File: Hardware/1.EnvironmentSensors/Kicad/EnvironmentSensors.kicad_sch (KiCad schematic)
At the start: 16 parts, among them J2 Conn_01x10_Pin, U1 SHT4x, U2 BME680, U3 LPS22HB

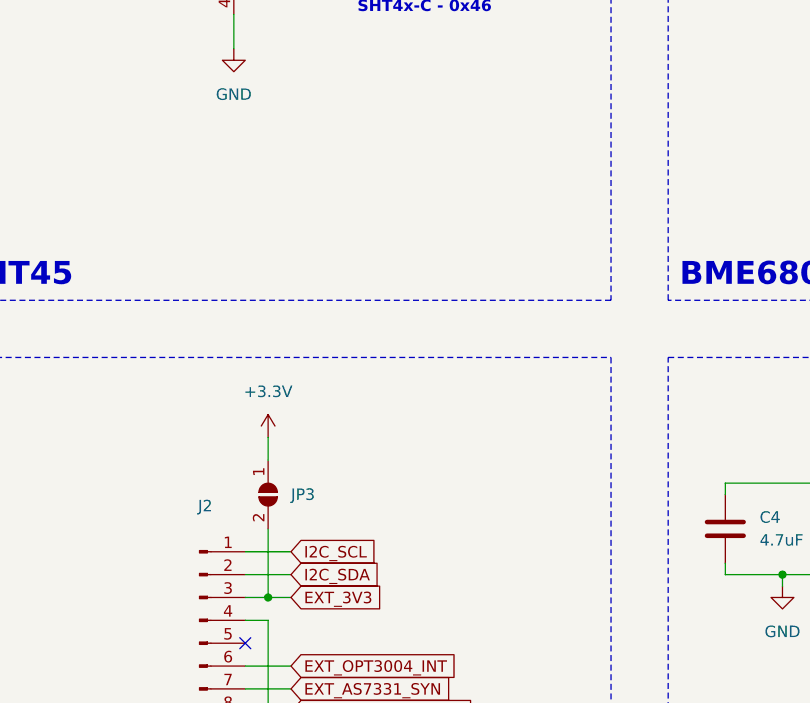
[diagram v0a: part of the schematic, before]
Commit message: Add SF2 filter to schematic
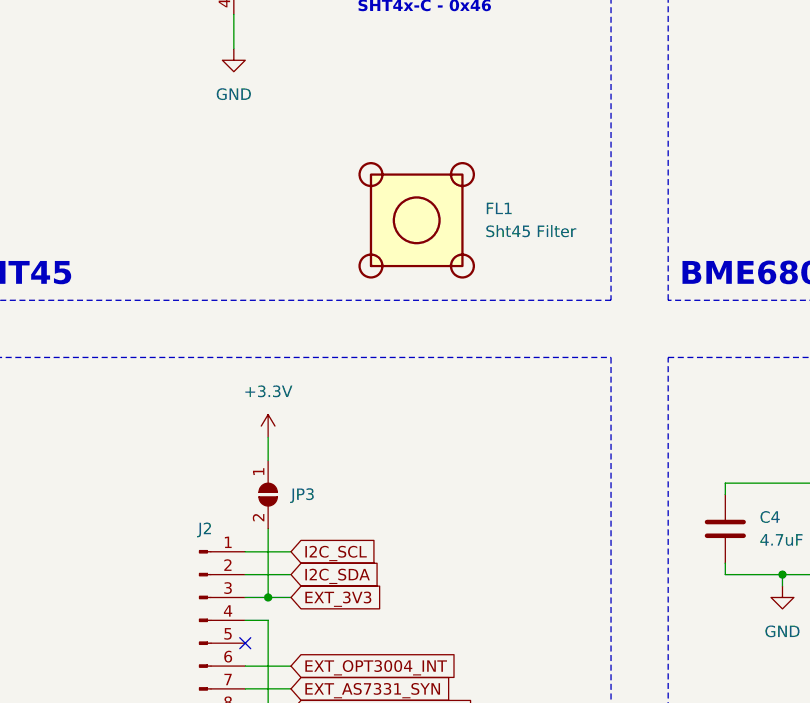
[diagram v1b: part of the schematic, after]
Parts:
- added FL1: Sht45 Filter, FIL_SF2_FILTER_CAP:FIL_SF2_FILTER_CAP, symbol SF2_FILTER_CAP:SF2_FILTER_CAP
- J2: footprint Connector_JST:JST_PH_S10B-PH-K_1x10_P2.00mm_Horizontal -> Connector_JST:JST_PH_B10B-PH-K_1x10_P2.00mm_Vertical
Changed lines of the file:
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@@
   (title_block
     (title "Enviroment Sensors")
-    (date "2023-07-30")
+    (date "2023-08-05")
     (rev "A")
   )
@@
     (pin "2")
     (instances
-      (project "EnviromentSensors"
+      (project "EnvironmentSensors"
         (path "/fc1a0c50-39ba-4cf6-ad6f-af313c028135"
           (reference "JP1") (unit 1)
@@
     (pin "1")
     (instances
-      (project "EnviromentSensors"
+      (project "EnvironmentSensors"
         (path "/fc1a0c50-39ba-4cf6-ad6f-af313c028135"
           (reference "#PWR08") (unit 1)
@@
     (pin "1")
     (instances
-      (project "EnviromentSensors"
+      (project "EnvironmentSensors"
         (path "/fc1a0c50-39ba-4cf6-ad6f-af313c028135"
           (reference "#PWR07") (unit 1)
@@
     (pin "1")
     (instances
-      (project "EnviromentSensors"
+      (project "EnvironmentSensors"
         (path "/fc1a0c50-39ba-4cf6-ad6f-af313c028135"
           (reference "#FLG02") (unit 1)
@@
     (pin "2")
     (instances
-      (project "EnviromentSensors"
+      (project "EnvironmentSensors"
         (path "/fc1a0c50-39ba-4cf6-ad6f-af313c028135"
           (reference "C1") (unit 1)
@@
     (pin "1")
     (instances
-      (project "EnviromentSensors"
+      (project "EnvironmentSensors"
         (path "/fc1a0c50-39ba-4cf6-ad6f-af313c028135"
           (reference "#PWR02") (unit 1)
@@
     )
   )
+  (symbol (lib_id "SF2_FILTER_CAP:SF2_FILTER_CAP") (at 133.35 73.66 0) (unit 1)
+    (in_bom yes) (on_board yes) (dnp no) (fields_autoplaced)
+    (property "Reference" "FL1" (at 140.97 72.39 0)
+      (effects (font (size 1.27 1.27)) (justify left))
+    )
+    (property "Value" "Sht45 Filter" (at 140.97 74.93 0)
+      (effects (font (size 1.27 1.27)) (justify left))
+    )
+    (property "Footprint" "FIL_SF2_FILTER_CAP:FIL_SF2_FILTER_CAP" (at 133.35 73.66 0)
+      (effects (font (size 1.27 1.27)) (justify bottom) hide)
+    )
+    (property "Datasheet" "" (at 133.35 73.66 0)
+      (effects (font (size 1.27 1.27)) hide)
+    )
+    (property "MANUFACTURER" "Sensirion" (at 133.35 73.66 0)
+      (effects (font (size 1.27 1.27)) (justify bottom) hide)
+    )
+    (instances
+      (project "EnvironmentSensors"
+        (path "/fc1a0c50-39ba-4cf6-ad6f-af313c028135"
+          (reference "FL1") (unit 1)
+        )
+      )
+    )
+  )
   (symbol (lib_id "power:GND") (at 173.99 114.3 0) (unit 1)
     (in_bom yes) (on_board yes) (dnp no) (fields_autoplaced)
@@
     (pin "1")
     (instances
-      (project "EnviromentSensors"
+      (project "EnvironmentSensors"
         (path "/fc1a0c50-39ba-4cf6-ad6f-af313c028135"
           (reference "#PWR014") (unit 1)
@@
     (pin "1")
     (instances
-      (project "EnviromentSensors"
+      (project "EnvironmentSensors"
         (path "/fc1a0c50-39ba-4cf6-ad6f-af313c028135"
           (reference "#PWR013") (unit 1)
@@
     (pin "1")
     (instances
-      (project "EnviromentSensors"
+      (project "EnvironmentSensors"
         (path "/fc1a0c50-39ba-4cf6-ad6f-af313c028135"
           (reference "#FLG01") (unit 1)
@@
     (pin "1")
     (instances
-      (project "EnviromentSensors"
+      (project "EnvironmentSensors"
         (path "/fc1a0c50-39ba-4cf6-ad6f-af313c028135"
           (reference "#PWR011") (unit 1)
@@
   (symbol (lib_id "Connector:Conn_01x10_Pin") (at 109.22 120.65 0) (unit 1)
     (in_bom yes) (on_board yes) (dnp no) (fields_autoplaced)
-    (property "Reference" "J2" (at 109.855 105.41 0)
+    (property "Reference" "J2" (at 109.855 107.95 0)
       (effects (font (size 1.27 1.27)))
     )
@@
         )
       )
-      (project "EnviromentSensors"
-        (path "/fc1a0c50-39ba-4cf6-ad6f-af313c028135"
-          (reference "J3") (unit 1)
+      (project "EnvironmentSensors"
+        (path "/fc1a0c50-39ba-4cf6-ad6f-af313c028135"
+          (reference "J2") (unit 1)
         )
       )
@@
     (pin "1")
     (instances
-      (project "EnviromentSensors"
+      (project "EnvironmentSensors"
         (path "/fc1a0c50-39ba-4cf6-ad6f-af313c028135"
           (reference "#PWR04") (unit 1)
@@
       (effects (font (size 1.27 1.27)) hide)
     )
-    (property "Footprint" "Connector_JST:JST_PH_S10B-PH-K_1x10_P2.00mm_Horizontal" (at 26.67 52.07 0)
+    (property "Footprint" "Connector_JST:JST_PH_B10B-PH-K_1x10_P2.00mm_Vertical" (at 26.67 52.07 0)
       (effects (font (size 1.27 1.27)) hide)
     )
@@
         )
       )
-      (project "EnviromentSensors"
+      (project "EnvironmentSensors"
         (path "/fc1a0c50-39ba-4cf6-ad6f-af313c028135"
           (reference "J1") (unit 1)
@@
     (pin "2")
     (instances
-      (project "EnviromentSensors"
+      (project "EnvironmentSensors"
         (path "/fc1a0c50-39ba-4cf6-ad6f-af313c028135"
           (reference "JP3") (unit 1)
@@
     (pin "1")
     (instances
-      (project "EnviromentSensors"
+      (project "EnvironmentSensors"
         (path "/fc1a0c50-39ba-4cf6-ad6f-af313c028135"
           (reference "#PWR015") (unit 1)
@@
     (pin "1")
     (instances
-      (project "EnviromentSensors"
+      (project "EnvironmentSensors"
         (path "/fc1a0c50-39ba-4cf6-ad6f-af313c028135"
           (reference "#PWR05") (unit 1)
@@
     (pin "2")
     (instances
-      (project "EnviromentSensors"
+      (project "EnvironmentSensors"
         (path "/fc1a0c50-39ba-4cf6-ad6f-af313c028135"
           (reference "R3") (unit 1)
@@
     (pin "1")
     (instances
-      (project "EnviromentSensors"
+      (project "EnvironmentSensors"
         (path "/fc1a0c50-39ba-4cf6-ad6f-af313c028135"
           (reference "#PWR09") (unit 1)
@@
     (pin "2")
     (instances
-      (project "EnviromentSensors"
+      (project "EnvironmentSensors"
         (path "/fc1a0c50-39ba-4cf6-ad6f-af313c028135"
           (reference "R2") (unit 1)
@@
     (pin "9")
     (instances
-      (project "EnviromentSensors"
+      (project "EnvironmentSensors"
         (path "/fc1a0c50-39ba-4cf6-ad6f-af313c028135"
           (reference "U3") (unit 1)
@@
     (pin "1")
     (instances
-      (project "EnviromentSensors"
+      (project "EnvironmentSensors"
         (path "/fc1a0c50-39ba-4cf6-ad6f-af313c028135"
           (reference "#PWR06") (unit 1)
@@
     (pin "1")
     (instances
-      (project "EnviromentSensors"
+      (project "EnvironmentSensors"
         (path "/fc1a0c50-39ba-4cf6-ad6f-af313c028135"
           (reference "#PWR012") (unit 1)
@@
         )
       )
-      (project "EnviromentSensors"
+      (project "EnvironmentSensors"
         (path "/fc1a0c50-39ba-4cf6-ad6f-af313c028135"
           (reference "#PWR018") (unit 1)
@@
     (pin "2")
     (instances
-      (project "EnviromentSensors"
+      (project "EnvironmentSensors"
         (path "/fc1a0c50-39ba-4cf6-ad6f-af313c028135"
           (reference "R1") (unit 1)
@@
     (pin "1")
     (instances
-      (project "EnviromentSensors"
+      (project "EnvironmentSensors"
         (path "/fc1a0c50-39ba-4cf6-ad6f-af313c028135"
           (reference "#PWR010") (unit 1)
@@
     (pin "2")
     (instances
-      (project "EnviromentSensors"
+      (project "EnvironmentSensors"
         (path "/fc1a0c50-39ba-4cf6-ad6f-af313c028135"
           (reference "C2") (unit 1)
@@
     (pin "8")
     (instances
-      (project "EnviromentSensors"
+      (project "EnvironmentSensors"
         (path "/fc1a0c50-39ba-4cf6-ad6f-af313c028135"
           (reference "U2") (unit 1)
@@
     (pin "2")
     (instances
-      (project "EnviromentSensors"
+      (project "EnvironmentSensors"
         (path "/fc1a0c50-39ba-4cf6-ad6f-af313c028135"
           (reference "R4") (unit 1)
@@
     (pin "1")
     (instances
-      (project "EnviromentSensors"
+      (project "EnvironmentSensors"
         (path "/fc1a0c50-39ba-4cf6-ad6f-af313c028135"
           (reference "#PWR016") (unit 1)
@@
     (pin "1")
     (instances
-      (project "EnviromentSensors"
+      (project "EnvironmentSensors"
         (path "/fc1a0c50-39ba-4cf6-ad6f-af313c028135"
           (reference "#PWR01") (unit 1)
@@
     (pin "2")
     (instances
-      (project "EnviromentSensors"
+      (project "EnvironmentSensors"
         (path "/fc1a0c50-39ba-4cf6-ad6f-af313c028135"
           (reference "C4") (unit 1)
@@
     (pin "1")
     (instances
-      (project "EnviromentSensors"
+      (project "EnvironmentSensors"
         (path "/fc1a0c50-39ba-4cf6-ad6f-af313c028135"
           (reference "#PWR017") (unit 1)
@@
     (pin "2")
     (instances
-      (project "EnviromentSensors"
+      (project "EnvironmentSensors"
         (path "/fc1a0c50-39ba-4cf6-ad6f-af313c028135"
           (reference "JP2") (unit 1)
@@
     (pin "1")
     (instances
-      (project "EnviromentSensors"
+      (project "EnvironmentSensors"
         (path "/fc1a0c50-39ba-4cf6-ad6f-af313c028135"
           (reference "#PWR03") (unit 1)
@@
     (pin "2")
     (instances
-      (project "EnviromentSensors"
+      (project "EnvironmentSensors"
         (path "/fc1a0c50-39ba-4cf6-ad6f-af313c028135"
           (reference "C3") (unit 1)
@@
     (pin "4")
     (instances
-      (project "EnviromentSensors"
+      (project "EnvironmentSensors"
         (path "/fc1a0c50-39ba-4cf6-ad6f-af313c028135"
           (reference "U1") (unit 1)

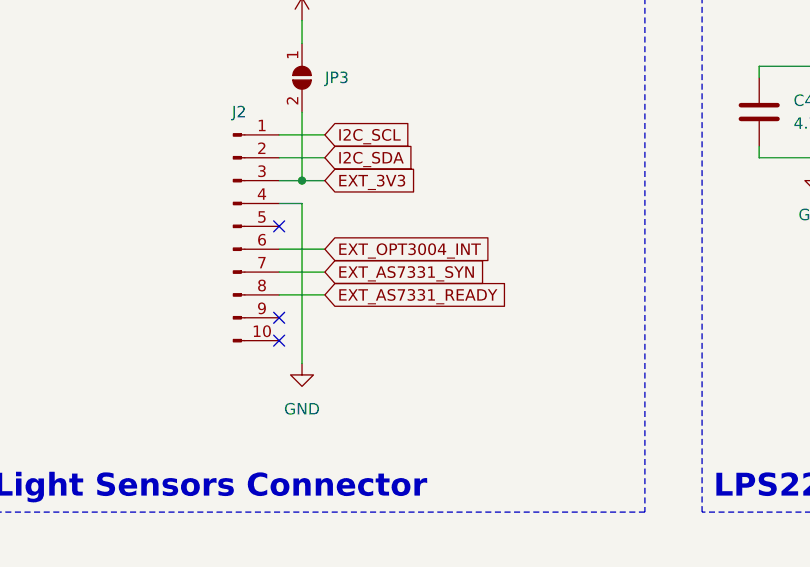
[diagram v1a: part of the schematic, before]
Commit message: Change footprint for connectors
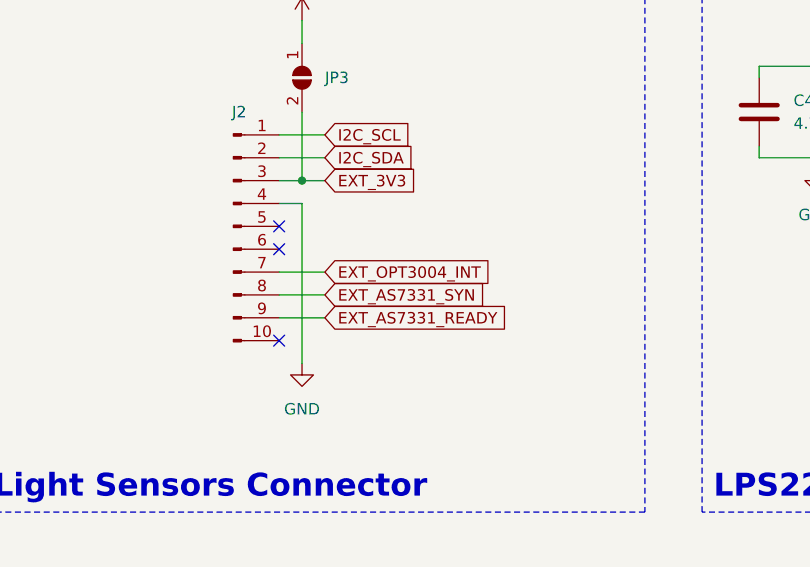
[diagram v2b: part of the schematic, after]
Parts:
- J2: footprint Connector_JST:JST_PH_B10B-PH-K_1x10_P2.00mm_Vertical -> Connector_JST:JST_PH_B10B-PH-SM4-TB_1x10-1MP_P2.00mm_Vertical
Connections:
- net EXT_AS7331_READY: now also J2.9 (Pin_9); no longer J2.8 (Pin_8)
- net EXT_AS7331_SYN: now also J2.8 (Pin_8); no longer J2.7 (Pin_7)
- net EXT_OPT3004_INT: now also J2.7 (Pin_7); no longer J2.6 (Pin_6)
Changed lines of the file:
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@@
   (junction (at 39.37 31.75) (diameter 0) (color 0 0 0 0)
   )
+  (no_connect (at 114.3 123.19))
   (no_connect (at 114.3 133.35))
   (no_connect (at 114.3 120.65))
-  (no_connect (at 114.3 130.81))
   (no_connect (at 31.75 64.77))
   (wire (pts (xy 205.74 66.04) (xy 205.74 64.77))
@@
     (stroke (width 0) (type default))
   )
+  (wire (pts (xy 102.87 45.72) (xy 99.06 45.72))
+    (stroke (width 0) (type default))
+  )
+  (wire (pts (xy 39.37 40.64) (xy 39.37 41.91))
+    (stroke (width 0) (type default))
+  )
   (wire (pts (xy 119.38 128.27) (xy 114.3 128.27))
     (stroke (width 0) (type default))
   )
-  (wire (pts (xy 102.87 45.72) (xy 99.06 45.72))
-    (stroke (width 0) (type default))
-  )
-  (wire (pts (xy 39.37 40.64) (xy 39.37 41.91))
-    (stroke (width 0) (type default))
-  )
   (wire (pts (xy 217.17 111.76) (xy 238.76 111.76))
     (stroke (width 0) (type default))
@@
     (stroke (width 0) (type default))
   )
-  (wire (pts (xy 119.38 123.19) (xy 114.3 123.19))
-    (stroke (width 0) (type default))
-  )
   (wire (pts (xy 26.67 189.23) (xy 26.67 186.69))
     (stroke (width 0) (type default))
@@
     (stroke (width 0) (type default))
   )
+  (wire (pts (xy 119.38 130.81) (xy 114.3 130.81))
+    (stroke (width 0) (type default))
+  )
   (wire (pts (xy 48.26 44.45) (xy 50.8 44.45))
     (stroke (width 0) (type default))
   )
+  (wire (pts (xy 119.38 125.73) (xy 114.3 125.73))
+    (stroke (width 0) (type default))
+  )
   (wire (pts (xy 173.99 31.75) (xy 185.42 31.75))
-    (stroke (width 0) (type default))
-  )
-  (wire (pts (xy 119.38 125.73) (xy 114.3 125.73))
     (stroke (width 0) (type default))
   )
@@
     )
   )
-  (global_label "EXT_AS7331_READY" (shape input) (at 119.38 128.27 0) (fields_autoplaced)
-    (effects (font (size 1.27 1.27)) (justify left))
-    (property "Intersheetrefs" "${INTERSHEET_REFS}" (at 140.6288 128.27 0)
+  (global_label "EXT_AS7331_READY" (shape input) (at 119.38 130.81 0) (fields_autoplaced)
+    (effects (font (size 1.27 1.27)) (justify left))
+    (property "Intersheetrefs" "${INTERSHEET_REFS}" (at 140.6288 130.81 0)
       (effects (font (size 1.27 1.27)) (justify left) hide)
     )
@@
     )
   )
-  (global_label "EXT_OPT3004_INT" (shape input) (at 119.38 123.19 0) (fields_autoplaced)
-    (effects (font (size 1.27 1.27)) (justify left))
-    (property "Intersheetrefs" "${INTERSHEET_REFS}" (at 138.9355 123.19 0)
-      (effects (font (size 1.27 1.27)) (justify left) hide)
-    )
-  )
-  (global_label "EXT_AS7331_SYN" (shape input) (at 119.38 125.73 0) (fields_autoplaced)
-    (effects (font (size 1.27 1.27)) (justify left))
-    (property "Intersheetrefs" "${INTERSHEET_REFS}" (at 138.3912 125.73 0)
+  (global_label "EXT_OPT3004_INT" (shape input) (at 119.38 125.73 0) (fields_autoplaced)
+    (effects (font (size 1.27 1.27)) (justify left))
+    (property "Intersheetrefs" "${INTERSHEET_REFS}" (at 138.9355 125.73 0)
+      (effects (font (size 1.27 1.27)) (justify left) hide)
+    )
+  )
+  (global_label "EXT_AS7331_SYN" (shape input) (at 119.38 128.27 0) (fields_autoplaced)
+    (effects (font (size 1.27 1.27)) (justify left))
+    (property "Intersheetrefs" "${INTERSHEET_REFS}" (at 138.3912 128.27 0)
       (effects (font (size 1.27 1.27)) (justify left) hide)
     )
@@
       (effects (font (size 1.27 1.27)) hide)
     )
-    (property "Footprint" "Connector_JST:JST_PH_B10B-PH-K_1x10_P2.00mm_Vertical" (at 109.22 120.65 0)
+    (property "Footprint" "Connector_JST:JST_PH_B10B-PH-SM4-TB_1x10-1MP_P2.00mm_Vertical" (at 109.22 120.65 0)
       (effects (font (size 1.27 1.27)) hide)
     )
@@
       (effects (font (size 1.27 1.27)) hide)
     )
-    (property "Footprint" "Connector_JST:JST_PH_B10B-PH-K_1x10_P2.00mm_Vertical" (at 26.67 52.07 0)
-      (effects (font (size 1.27 1.27)) hide)
-    )
+    (property "Footprint" "Connector_JST:JST_PH_B10B-PH-SM4-TB_1x10-1MP_P2.00mm_Vertical" (at 26.67 52.07 0)
+      (effects (font (size 1.27 1.27)) hide)
+    )

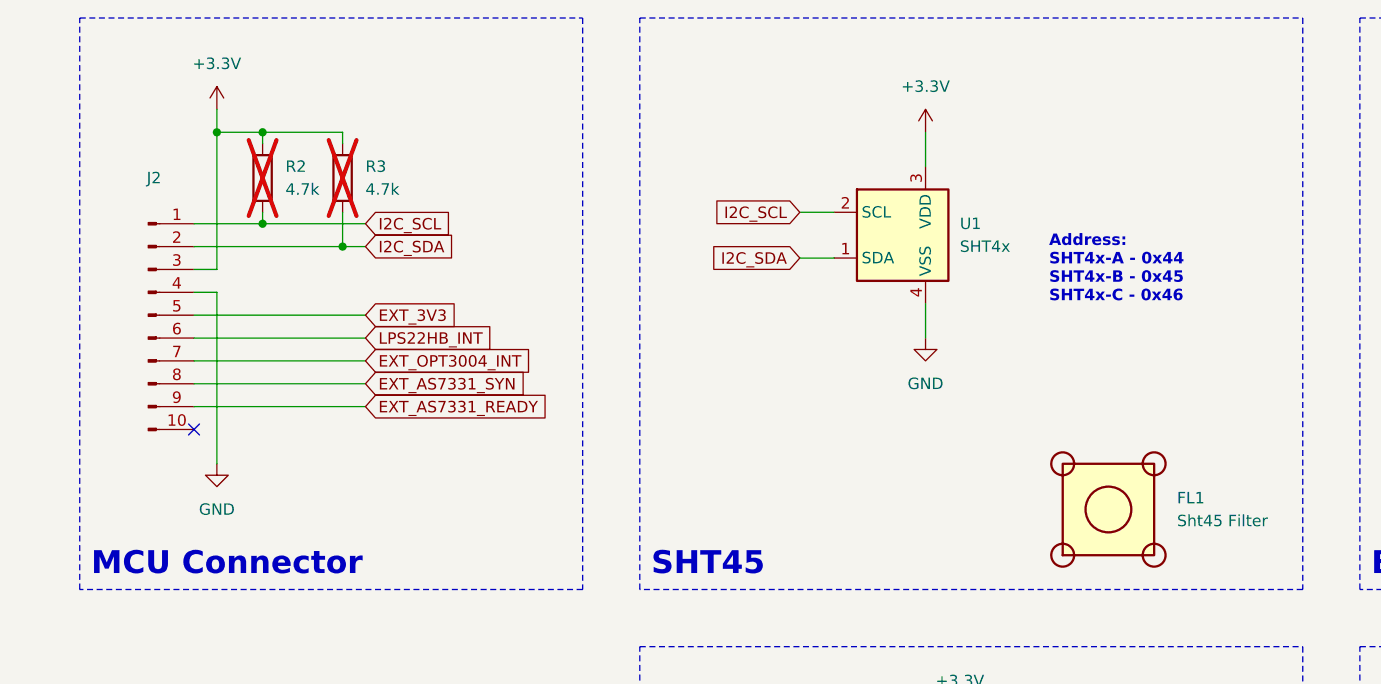
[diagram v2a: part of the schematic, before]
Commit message: Add capacitor for supply connector, SHT21 and change resistors and capacitors footprint to 0603
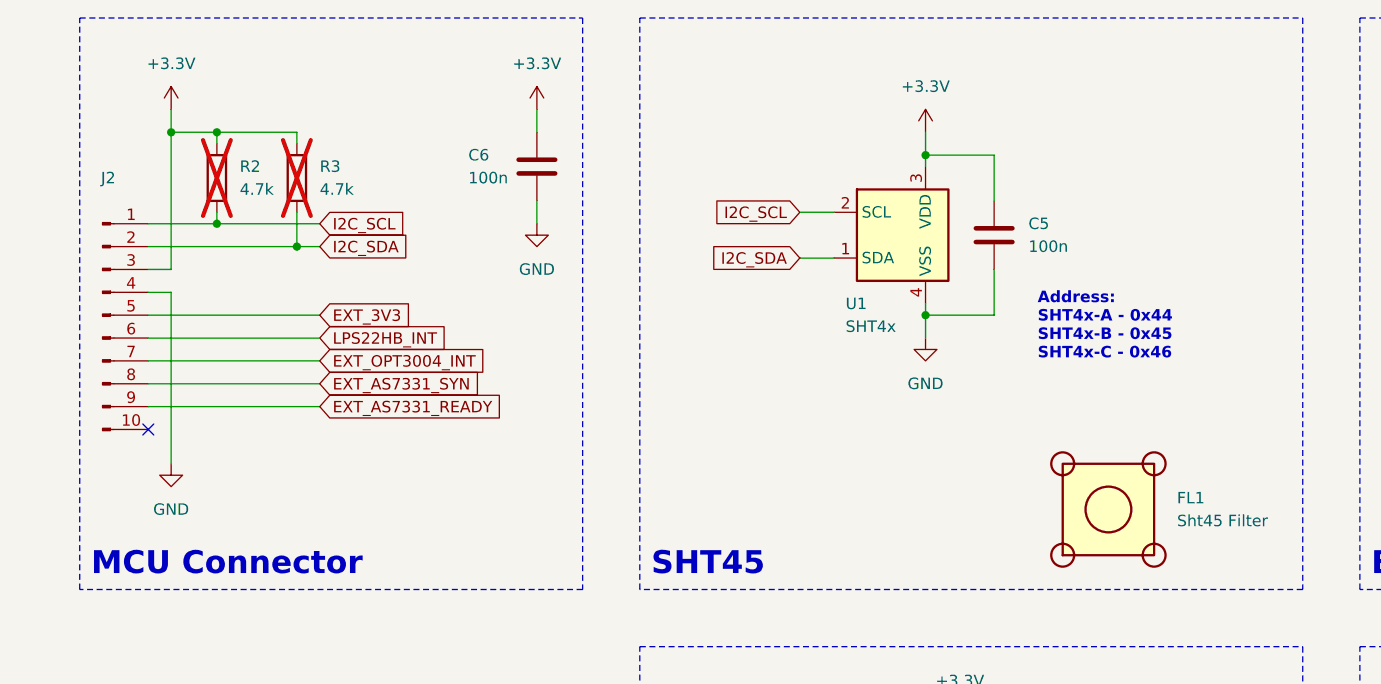
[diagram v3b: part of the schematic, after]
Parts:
- added C5, C6: 100n, Capacitor_SMD:C_0603_1608Metric, symbol Device:C
- C1, C2, C3, C4: footprint Capacitor_SMD:C_0402_1005Metric -> Capacitor_SMD:C_0603_1608Metric
- R1, R2, R3, R4: footprint Resistor_SMD:R_0402_1005Metric -> Resistor_SMD:R_0603_1608Metric
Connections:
- net +3.3V: now also C5.1, C6.1
- net GND: now also C5.2, C6.2
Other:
- moved on the sheet: J2, R2, R3

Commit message: Update schematic date
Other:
- company: (none) -> Github.com/L0R3nz
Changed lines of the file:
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@@
   (title_block
     (title "Enviroment Sensors")
-    (date "2023-08-05")
+    (date "2023-09-03")
     (rev "A")
+    (company "Github.com/L0R3nz")
   )
   (junction (at 203.2 31.75) (diameter 0) (color 0 0 0 0)
